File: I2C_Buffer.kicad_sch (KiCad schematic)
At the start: 6 parts, among them U2 LTC4300A-1IMS8_PBF

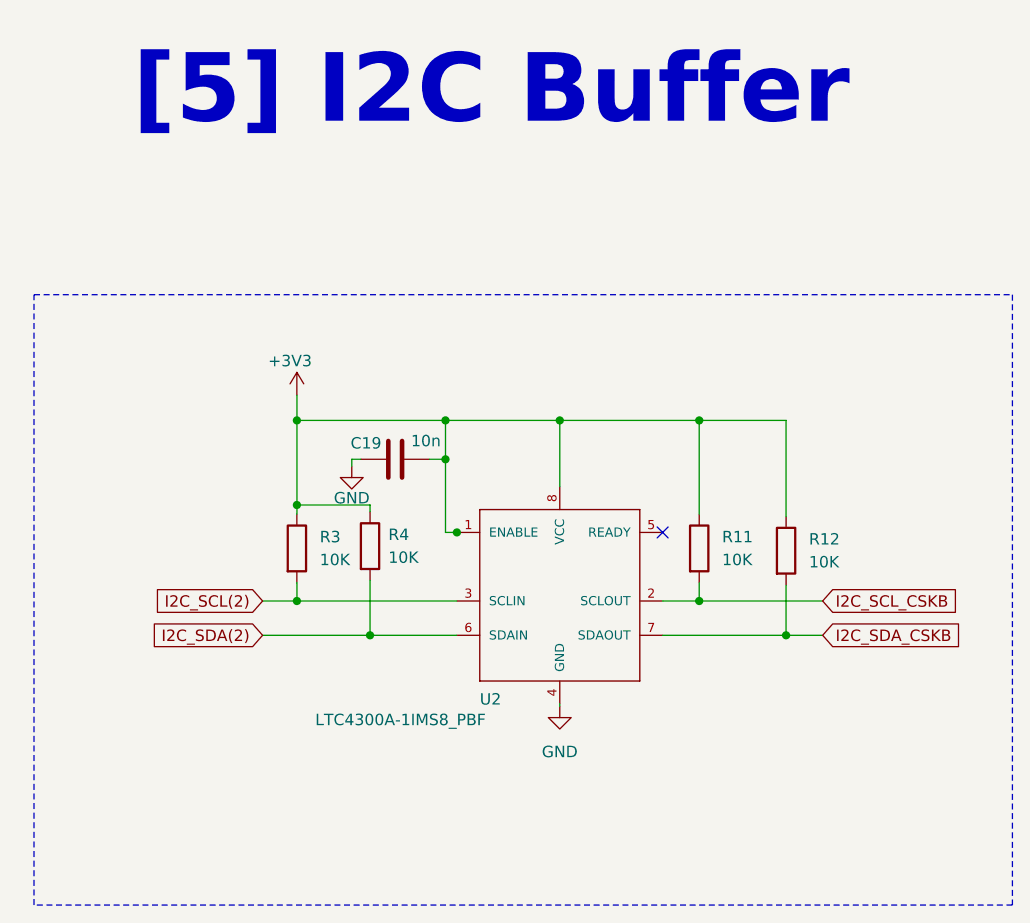
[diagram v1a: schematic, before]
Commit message: Added Level Shifter for SD card
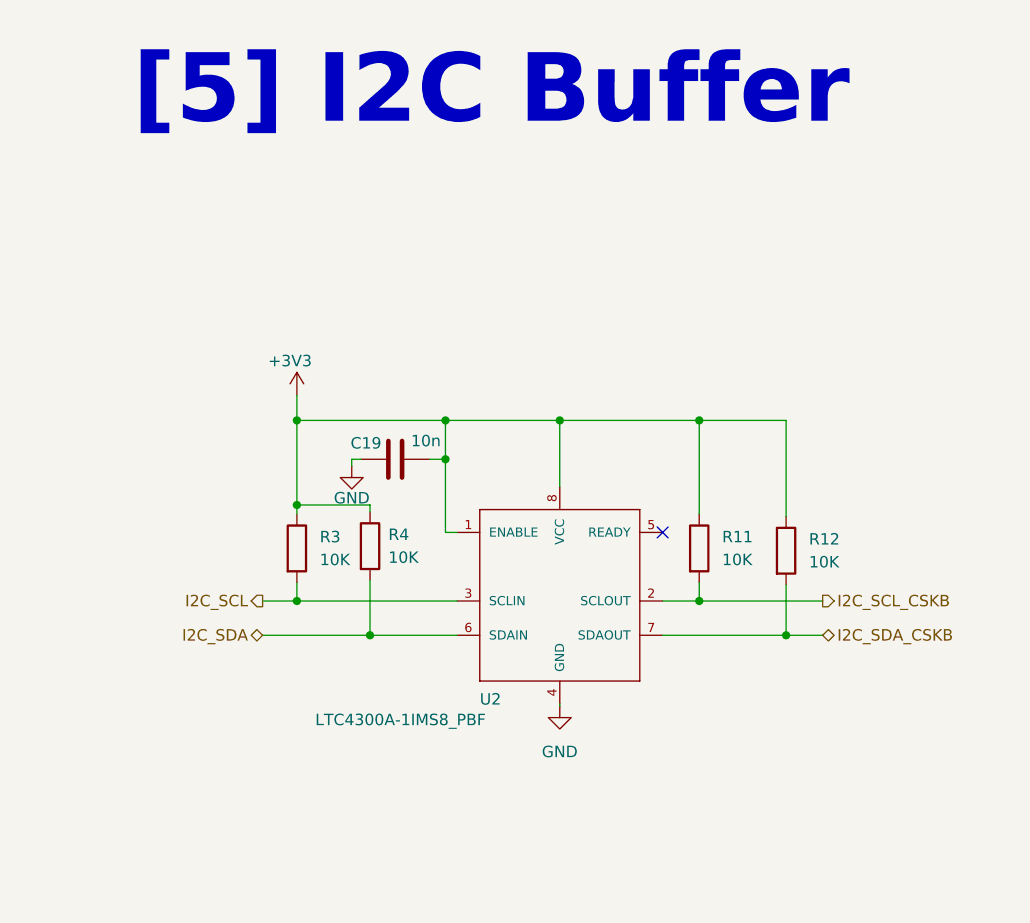
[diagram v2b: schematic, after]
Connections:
- net I2C_SCL(2) renamed I2C_SCL
- net I2C_SDA(2) renamed I2C_SDA
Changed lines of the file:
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@@
 	(generator_version "10.0")
 	(paper "A4")
-	(rectangle
-		(start 91.44 48.514)
-		(end 200.152 116.332)
-		(stroke
-			(width 0)
-			(type dash)
-		)
-		(fill
-			(type none)
-		)
-	)
 	(text "[5] I2C Buffer"
 		(exclude_from_sim no)
@@
 	)
 	(junction
-		(at 138.43 74.93)
-		(diameter 0)
-		(color 0 0 0 0)
-	)
-	(junction
 		(at 120.65 71.882)
 		(diameter 0)
@@
 	)
 	(junction
+		(at 149.86 62.484)
+		(diameter 0)
+		(color 0 0 0 0)
+	)
+	(junction
+		(at 165.354 82.55)
+		(diameter 0)
+		(color 0 0 0 0)
+	)
+	(junction
+		(at 120.65 62.484)
+		(diameter 0)
+		(color 0 0 0 0)
+	)
+	(junction
+		(at 175.006 86.36)
+		(diameter 0)
+		(color 0 0 0 0)
+	)
+	(junction
+		(at 120.65 82.55)
+		(diameter 0)
+		(color 0 0 0 0)
+	)
+	(junction
 		(at 137.16 66.802)
-		(diameter 0)
-		(color 0 0 0 0)
-	)
-	(junction
-		(at 149.86 62.484)
-		(diameter 0)
-		(color 0 0 0 0)
-	)
-	(junction
-		(at 165.354 82.55)
-		(diameter 0)
-		(color 0 0 0 0)
-	)
-	(junction
-		(at 120.65 62.484)
-		(diameter 0)
-		(color 0 0 0 0)
-	)
-	(junction
-		(at 175.006 86.36)
-		(diameter 0)
-		(color 0 0 0 0)
-	)
-	(junction
-		(at 120.65 82.55)
 		(diameter 0)
 		(color 0 0 0 0)
@@
 	(wire
 		(pts
-			(xy 138.43 74.93) (xy 137.16 74.93)
+			(xy 137.16 74.93) (xy 138.43 74.93)
 		)
 		(stroke
@@
 	(wire
 		(pts
-			(xy 138.684 74.93) (xy 138.43 74.93)
-		)
-		(stroke
-			(width 0)
-			(type default)
-		)
-	)
-	(wire
-		(pts
 			(xy 128.778 71.882) (xy 128.778 72.644)
 		)
@@
 		)
 	)
-	(global_label "I2C_SDA(2)"
-		(shape input)
+	(hierarchical_label "I2C_SDA_CSKB"
+		(shape bidirectional)
+		(at 179.07 86.36 0)
+		(effects
+			(font
+				(size 1.27 1.27)
+			)
+			(justify left)
+		)
+	)
+	(hierarchical_label "I2C_SDA"
+		(shape bidirectional)
 		(at 116.84 86.36 180)
-		(fields_autoplaced yes)
 		(effects
 			(font
@@
 			(justify right)
 		)
-		(property "Intersheetrefs" "${INTERSHEET_REFS}"
-			(at 103.3319 86.36 0)
-			(hide yes)
-			(show_name no)
-			(do_not_autoplace no)
-			(effects
-				(font
-					(size 1.27 1.27)
-				)
-				(justify right)
-			)
-		)
-	)
-	(global_label "I2C_SCL(2)"
-		(shape input)
+	)
+	(hierarchical_label "I2C_SCL_CSKB"
+		(shape output)
+		(at 179.07 82.55 0)
+		(effects
+			(font
+				(size 1.27 1.27)
+			)
+			(justify left)
+		)
+	)
+	(hierarchical_label "I2C_SCL"
+		(shape output)
 		(at 116.84 82.55 180)
-		(fields_autoplaced yes)
 		(effects
 			(font
@@
 			(justify right)
 		)
-		(property "Intersheetrefs" "${INTERSHEET_REFS}"
-			(at 103.3924 82.55 0)
-			(hide yes)
-			(show_name no)
-			(do_not_autoplace no)
-			(effects
-				(font
-					(size 1.27 1.27)
-				)
-				(justify right)
-			)
-		)
-	)
-	(global_label "I2C_SDA_CSKB"
-		(shape input)
-		(at 179.07 86.36 0)
-		(fields_autoplaced yes)
-		(effects
-			(font
-				(size 1.27 1.27)
-			)
-			(justify left)
-		)
-		(property "Intersheetrefs" "${INTERSHEET_REFS}"
-			(at 195.6623 86.36 0)
-			(hide yes)
-			(show_name no)
-			(do_not_autoplace no)
-			(effects
-				(font
-					(size 1.27 1.27)
-				)
-				(justify left)
-			)
-		)
-	)
-	(global_label "I2C_SCL_CSKB"
-		(shape input)
-		(at 179.07 82.55 0)
-		(fields_autoplaced yes)
-		(effects
-			(font
-				(size 1.27 1.27)
-			)
-			(justify left)
-		)
-		(property "Intersheetrefs" "${INTERSHEET_REFS}"
-			(at 195.6018 82.55 0)
-			(hide yes)
-			(show_name no)
-			(do_not_autoplace no)
-			(effects
-				(font
-					(size 1.27 1.27)
-				)
-				(justify left)
-			)
-		)
-	)
+	)

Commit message: Added pcb files for ethernet breakout board
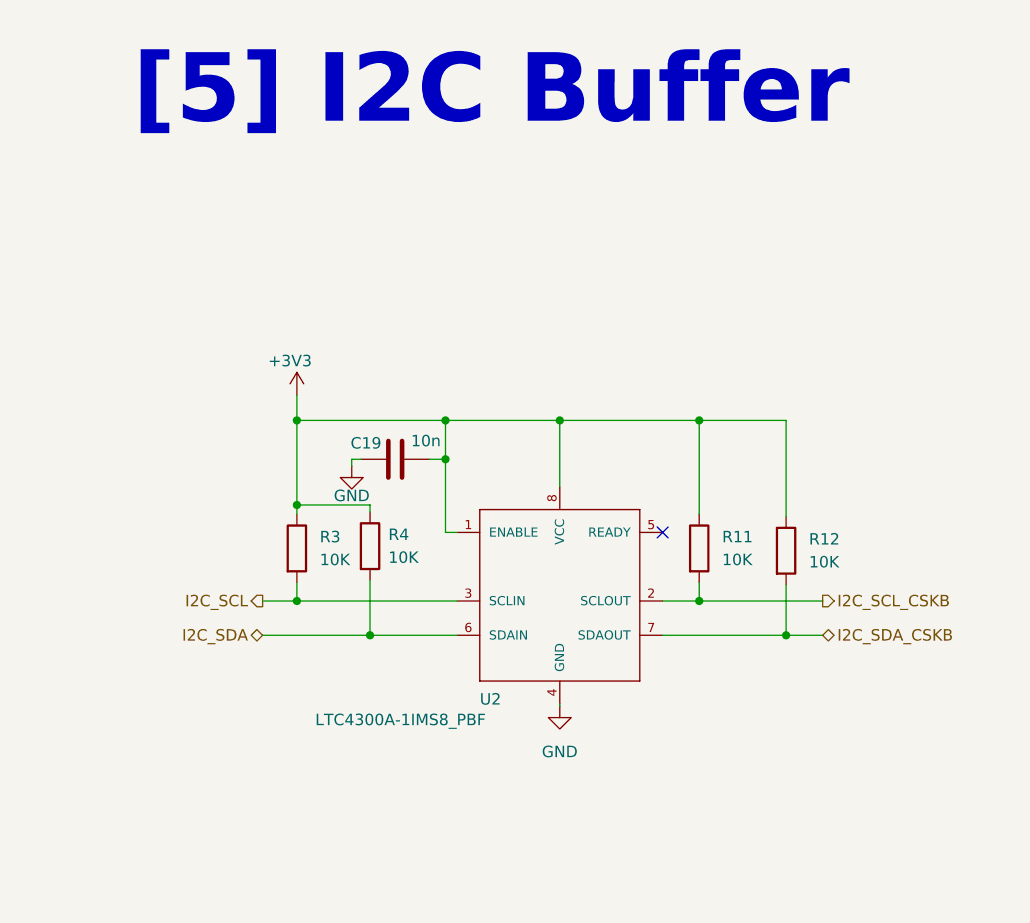
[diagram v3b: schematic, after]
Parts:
- U2: External Part Number (none) -> 584-C4300A-1IMS8PBF; MPN (none) -> C580853
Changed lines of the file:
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@@
+			)
+		)
+		(property "External Part Number" ""
+			(at 175.006 76.962 0)
+			(hide yes)
+			(show_name no)
+			(do_not_autoplace no)
+			(effects
+				(font
+					(size 1.27 1.27)
+				)
+			)
+		)
+		(property "MPN" ""
+			(at 175.006 76.962 0)
+			(hide yes)
+			(show_name no)
+			(do_not_autoplace no)
+			(effects
+				(font
+					(size 1.27 1.27)
+				)
 			)
 		)
@@
 		)
 		(property "Value" "GND"
-			(at 126.746 71.12 0)
+			(at 126.746 70.866 0)
 			(show_name no)
 			(do_not_autoplace no)
@@
 			)
 		)
-		(property "Datasheet" ""
+		(property "Datasheet" "https://www.analog.com/media/en/technical-documentation/data-sheets/4300a12fa.pdf"
 			(at 133.35 78.74 0)
 			(hide yes)
@@
 		)
 		(property "MANUFACTURER" "Analog Devices Inc."
+			(at 133.35 78.74 0)
+			(hide yes)
+			(show_name no)
+			(do_not_autoplace no)
+			(effects
+				(font
+					(size 1.27 1.27)
+				)
+			)
+		)
+		(property "External Part Number" "584-C4300A-1IMS8PBF"
+			(at 133.35 78.74 0)
+			(hide yes)
+			(show_name no)
+			(do_not_autoplace no)
+			(effects
+				(font
+					(size 1.27 1.27)
+				)
+			)
+		)
+		(property "MPN" "C580853"
 			(at 133.35 78.74 0)
 			(hide yes)
@@
 			)
 		)
+		(property "External Part Number" ""
+			(at 120.65 76.708 0)
+			(hide yes)
+			(show_name no)
+			(do_not_autoplace no)
+			(effects
+				(font
+					(size 1.27 1.27)
+				)
+			)
+		)
+		(property "MPN" ""
+			(at 120.65 76.708 0)
+			(hide yes)
+			(show_name no)
+			(do_not_autoplace no)
+			(effects
+				(font
+					(size 1.27 1.27)
+				)
+			)
+		)
 		(pin "1"
 		)
@@
 			)
 		)
+		(property "External Part Number" ""
+			(at 165.354 76.708 0)
+			(hide yes)
+			(show_name no)
+			(do_not_autoplace no)
+			(effects
+				(font
+					(size 1.27 1.27)
+				)
+			)
+		)
+		(property "MPN" ""
+			(at 165.354 76.708 0)
+			(hide yes)
+			(show_name no)
+			(do_not_autoplace no)
+			(effects
+				(font
+					(size 1.27 1.27)
+				)
+			)
+		)
 		(pin "1"
 		)
@@
 			)
 		)
+		(property "External Part Number" ""
+			(at 128.778 76.454 0)
+			(hide yes)
+			(show_name no)
+			(do_not_autoplace no)
+			(effects
+				(font
+					(size 1.27 1.27)
+				)
+			)
+		)
+		(property "MPN" ""
+			(at 128.778 76.454 0)
+			(hide yes)
+			(show_name no)
+			(do_not_autoplace no)
+			(effects
+				(font
+					(size 1.27 1.27)
+				)
+			)
+		)
 		(pin "1"
 		)
@@
 			(at 131.572 66.802 90)
 			(hide yes)
+			(show_name no)
+			(do_not_autoplace no)
+			(effects
+				(font
+					(size 1.27 1.27)
+				)
+			)
+		)
+		(property "External Part Number" ""
+			(at 131.572 66.802 90)
+			(hide yes)
+			(show_name no)
+			(do_not_autoplace no)
+			(effects
+				(font
+					(size 1.27 1.27)
+				)
+			)
+		)
+		(property "MPN" ""
+			(at 131.572 66.802 90)
+			(hide yes)

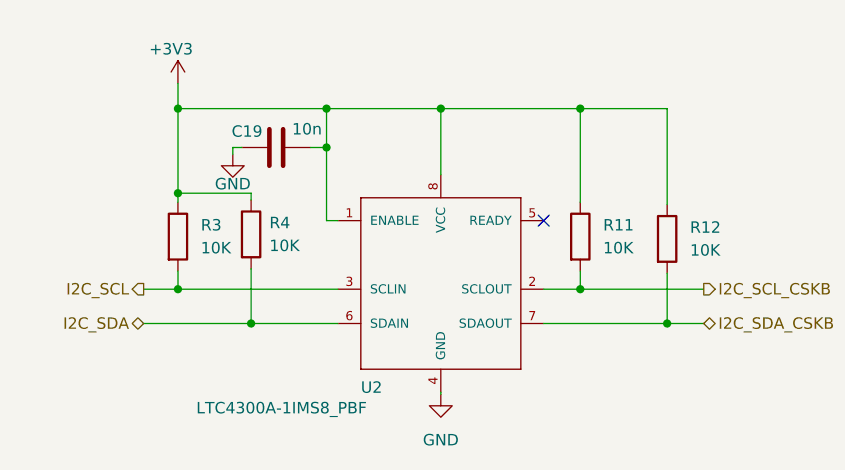
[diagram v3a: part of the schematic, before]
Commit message: Updated BOM and added fiducials
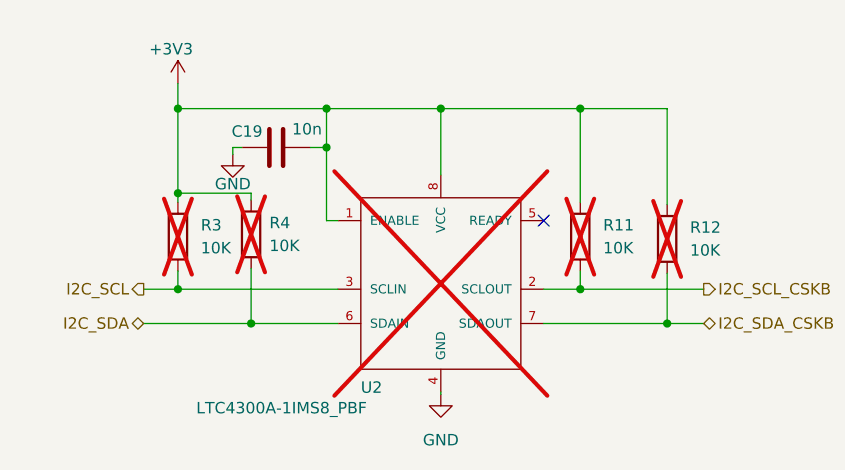
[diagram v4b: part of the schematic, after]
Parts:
- C19: External Part Number (none) -> GCM155R71H103KA55J; MANUFACTURER_PART_NUMBER GCM155R71H103KA55J -> (none); MPN (none) -> C2168451
- R11, R12, R3, R4: External Part Number (none) -> MCS0402MD1002BE100; MANUFACTURER_PART_NUMBER MCS0402MD1002BE100 -> (none); MPN (none) -> C2073498; now not fitted
- U2: External Part Number 584-C4300A-1IMS8PBF -> ltc4300a1ims8; MANUFACTURER_PART_NUMBER ltc4300a1ims8 -> (none); now not fitted
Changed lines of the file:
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@@
 		(on_board yes)
 		(in_pos_files yes)
-		(dnp no)
+		(dnp yes)
 		(fields_autoplaced yes)
 		(property "Reference" "R12"
@@
 			)
 		)
-		(property "MANUFACTURER_PART_NUMBER" "MCS0402MD1002BE100"
+		(property "External Part Number" "MCS0402MD1002BE100"
 			(at 175.006 76.962 0)
 			(hide yes)
@@
 			)
 		)
-		(property "External Part Number" ""
-			(at 175.006 76.962 0)
-			(hide yes)
-			(show_name no)
-			(do_not_autoplace no)
-			(effects
-				(font
-					(size 1.27 1.27)
-				)
-			)
-		)
-		(property "MPN" ""
+		(property "MPN" "C2073498"
 			(at 175.006 76.962 0)
 			(hide yes)
@@
 		(on_board yes)
 		(in_pos_files yes)
-		(dnp no)
+		(dnp yes)
 		(property "Reference" "U2"
 			(at 140.97 93.472 0)
@@
 			)
 		)
-		(property "MANUFACTURER_PART_NUMBER" "ltc4300a1ims8"
-			(at 131.572 63.5 0)
-			(hide yes)
-			(show_name no)
-			(do_not_autoplace no)
-			(effects
-				(font
-					(size 1.27 1.27)
-				)
-				(justify bottom)
-			)
-		)
 		(property "MANUFACTURER" "Analog Devices Inc."
 			(at 133.35 78.74 0)
@@
 			)
 		)
-		(property "External Part Number" "584-C4300A-1IMS8PBF"
+		(property "External Part Number" "ltc4300a1ims8"
 			(at 133.35 78.74 0)
 			(hide yes)
@@
 		(on_board yes)
 		(in_pos_files yes)
-		(dnp no)
+		(dnp yes)
 		(fields_autoplaced yes)
 		(property "Reference" "R3"
@@
 			)
 		)
-		(property "MANUFACTURER_PART_NUMBER" "MCS0402MD1002BE100"
+		(property "External Part Number" "MCS0402MD1002BE100"
 			(at 120.65 76.708 0)
 			(hide yes)
@@
 			)
 		)
-		(property "External Part Number" ""
-			(at 120.65 76.708 0)
-			(hide yes)
-			(show_name no)
-			(do_not_autoplace no)
-			(effects
-				(font
-					(size 1.27 1.27)
-				)
-			)
-		)
-		(property "MPN" ""
+		(property "MPN" "C2073498"
 			(at 120.65 76.708 0)
 			(hide yes)
@@
 		(on_board yes)
 		(in_pos_files yes)
-		(dnp no)
+		(dnp yes)
 		(fields_autoplaced yes)
 		(property "Reference" "R11"
@@
 			)
 		)
-		(property "MANUFACTURER_PART_NUMBER" "MCS0402MD1002BE100"
+		(property "External Part Number" "MCS0402MD1002BE100"
 			(at 165.354 76.708 0)
 			(hide yes)
@@
 			)
 		)
-		(property "External Part Number" ""
-			(at 165.354 76.708 0)
-			(hide yes)
-			(show_name no)
-			(do_not_autoplace no)
-			(effects
-				(font
-					(size 1.27 1.27)
-				)
-			)
-		)
-		(property "MPN" ""
+		(property "MPN" "C2073498"
 			(at 165.354 76.708 0)
 			(hide yes)
@@
 		(on_board yes)
 		(in_pos_files yes)
-		(dnp no)
+		(dnp yes)
 		(fields_autoplaced yes)
 		(property "Reference" "R4"
@@
 			)
 		)
-		(property "MANUFACTURER_PART_NUMBER" "MCS0402MD1002BE100"
+		(property "External Part Number" "MCS0402MD1002BE100"
 			(at 128.778 76.454 0)
 			(hide yes)
@@
 			)
 		)
-		(property "External Part Number" ""
-			(at 128.778 76.454 0)
-			(hide yes)
-			(show_name no)
-			(do_not_autoplace no)
-			(effects
-				(font
-					(size 1.27 1.27)
-				)
-			)
-		)
-		(property "MPN" ""
+		(property "MPN" "C2073498"
 			(at 128.778 76.454 0)
 			(hide yes)
@@
 			)
 		)
-		(property "MANUFACTURER_PART_NUMBER" "GCM155R71H103KA55J"
+		(property "External Part Number" "GCM155R71H103KA55J"
 			(at 131.572 66.802 90)
 			(hide yes)
@@
 			)
 		)
-		(property "External Part Number" ""
+		(property "MPN" "C2168451"
 			(at 131.572 66.802 90)
 			(hide yes)
-			(show_name no)
-			(do_not_autoplace no)
-			(effects
-				(font
-					(size 1.27 1.27)
-				)
-			)
-		)
-		(property "MPN" ""
-			(at 131.572 66.802 90)
-			(hide yes)

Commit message: added solder bridges and updated BOM
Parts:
- C19: External Part Num (none) -> C2168451; External Part Number GCM155R71H103KA55J -> (none); MPN C2168451 -> GCM155R71H103KA55J
- R11, R12, R3, R4: External Part Num (none) -> C2073498; External Part Number MCS0402MD1002BE100 -> (none); MPN C2073498 -> MCS0402MD1002BE100
- U2: External Part Num (none) -> C580853; External Part Number ltc4300a1ims8 -> (none); MPN C580853 -> ltc4300a1ims8
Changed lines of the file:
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@@
 			)
 		)
-		(property "External Part Number" "MCS0402MD1002BE100"
+		(property "MPN" "MCS0402MD1002BE100"
 			(at 175.006 76.962 0)
 			(hide yes)
@@
 			)
 		)
-		(property "MPN" "C2073498"
+		(property "External Part Num" "C2073498"
 			(at 175.006 76.962 0)
 			(hide yes)
@@
 			)
 		)
-		(property "External Part Number" "ltc4300a1ims8"
+		(property "MPN" "ltc4300a1ims8"
 			(at 133.35 78.74 0)
 			(hide yes)
@@
 			)
 		)
-		(property "MPN" "C580853"
+		(property "External Part Num" "C580853"
 			(at 133.35 78.74 0)
 			(hide yes)
@@
 			)
 		)
-		(property "External Part Number" "MCS0402MD1002BE100"
+		(property "MPN" "MCS0402MD1002BE100"
 			(at 120.65 76.708 0)
 			(hide yes)
@@
 			)
 		)
-		(property "MPN" "C2073498"
+		(property "External Part Num" "C2073498"
 			(at 120.65 76.708 0)
 			(hide yes)
@@
 			)
 		)
-		(property "External Part Number" "MCS0402MD1002BE100"
+		(property "MPN" "MCS0402MD1002BE100"
 			(at 165.354 76.708 0)
 			(hide yes)
@@
 			)
 		)
-		(property "MPN" "C2073498"
+		(property "External Part Num" "C2073498"
 			(at 165.354 76.708 0)
 			(hide yes)
@@
 			)
 		)
-		(property "External Part Number" "MCS0402MD1002BE100"
+		(property "MPN" "MCS0402MD1002BE100"
 			(at 128.778 76.454 0)
 			(hide yes)
@@
 			)
 		)
-		(property "MPN" "C2073498"
+		(property "External Part Num" "C2073498"
 			(at 128.778 76.454 0)
 			(hide yes)
@@
 			)
 		)
-		(property "External Part Number" "GCM155R71H103KA55J"
+		(property "MPN" "GCM155R71H103KA55J"
 			(at 131.572 66.802 90)
 			(hide yes)
@@
 			)
 		)
-		(property "MPN" "C2168451"
+		(property "External Part Num" "C2168451"
 			(at 131.572 66.802 90)
 			(hide yes)
